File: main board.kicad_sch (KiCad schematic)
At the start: 1 part

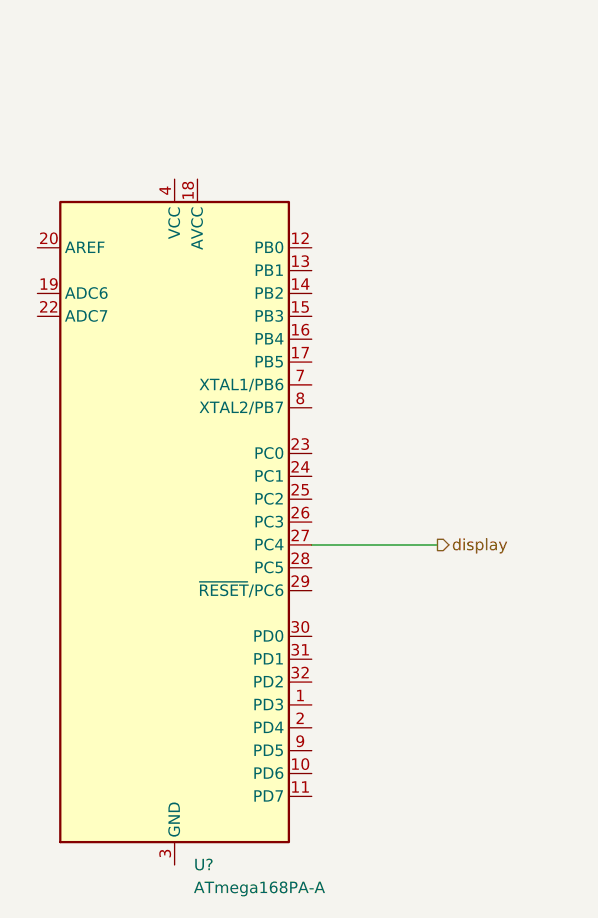
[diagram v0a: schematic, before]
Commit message: added display
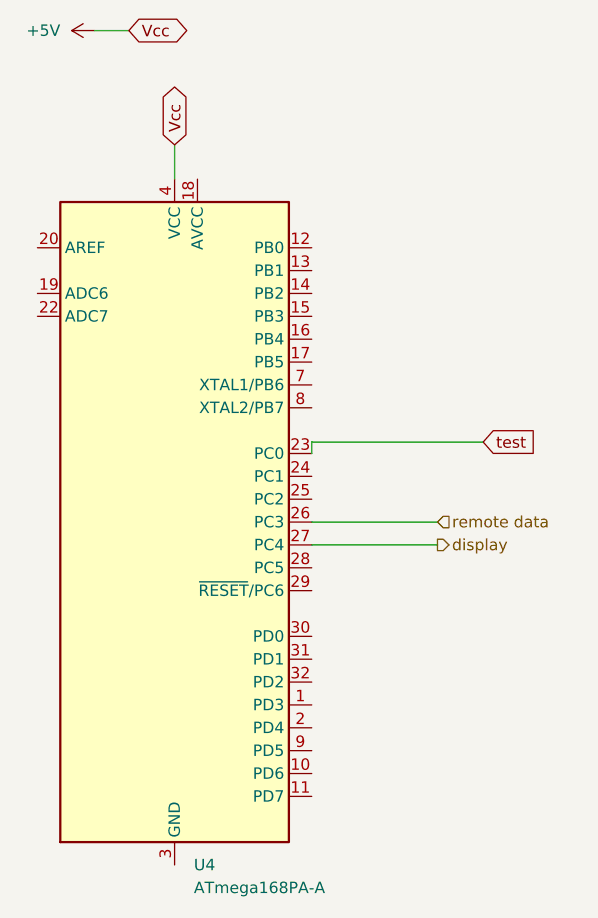
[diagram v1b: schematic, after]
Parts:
- gave numbers to parts that had none: 1
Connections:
- net test: now reaches U4.23 (PC0)
- net remote data: now reaches U4.26 (PC3)
- net +5V: now reaches U4.4 (VCC), U4.6 (VCC)
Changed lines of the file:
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@@
+	(wire
+		(pts
+			(xy 143.51 55.88) (xy 143.51 52.07)
+		)
+		(stroke
+			(width 0)
+			(type default)
+		)
+	)
+	(wire
+		(pts
+			(xy 134.62 39.37) (xy 138.43 39.37)
+		)
+		(stroke
+			(width 0)
+			(type default)
+		)
+	)
 	(wire
 		(pts
@@
 			(width 0)
 			(type default)
+		)
+	)
+	(wire
+		(pts
+			(xy 158.75 93.98) (xy 172.72 93.98)
+		)
+		(stroke
+			(width 0)
+			(type default)
+		)
+	)
+	(wire
+		(pts
+			(xy 158.75 85.09) (xy 158.75 86.36)
+		)
+		(stroke
+			(width 0)
+			(type default)
+		)
+	)
+	(wire
+		(pts
+			(xy 177.8 85.09) (xy 158.75 85.09)
+		)
+		(stroke
+			(width 0)
+			(type default)
+		)
+	)
+	(global_label "Vcc"
+		(shape bidirectional)
+		(at 138.43 39.37 0)
+		(fields_autoplaced yes)
+		(effects
+			(font
+				(size 1.27 1.27)
+			)
+			(justify left)
+		)
+		(property "Intersheetrefs" "${INTERSHEET_REFS}"
+			(at 145.7923 39.37 0)
+			(hide yes)
+			(show_name no)
+			(do_not_autoplace no)
+			(effects
+				(font
+					(size 1.27 1.27)
+				)
+				(justify left)
+			)
+		)
+	)
+	(global_label "test"
+		(shape input)
+		(at 177.8 85.09 0)
+		(fields_autoplaced yes)
+		(effects
+			(font
+				(size 1.27 1.27)
+			)
+			(justify left)
+		)
+		(property "Intersheetrefs" "${INTERSHEET_REFS}"
+			(at 184.3533 85.09 0)
+			(hide yes)
+			(show_name no)
+			(do_not_autoplace no)
+			(effects
+				(font
+					(size 1.27 1.27)
+				)
+				(justify left)
+			)
+		)
+	)
+	(global_label "Vcc"
+		(shape bidirectional)
+		(at 143.51 52.07 90)
+		(fields_autoplaced yes)
+		(effects
+			(font
+				(size 1.27 1.27)
+			)
+			(justify left)
+		)
+		(property "Intersheetrefs" "${INTERSHEET_REFS}"
+			(at 143.51 44.7077 90)
+			(hide yes)
+			(show_name no)
+			(do_not_autoplace no)
+			(effects
+				(font
+					(size 1.27 1.27)
+				)
+				(justify left)
+			)
 		)
 	)
@@
 		(shape output)
 		(at 172.72 96.52 0)
+		(effects
+			(font
+				(size 1.27 1.27)
+			)
+			(justify left)
+		)
+	)
+	(hierarchical_label "remote data"
+		(shape input)
+		(at 172.72 93.98 0)
 		(effects
 			(font
@@
 		(dnp no)
 		(fields_autoplaced yes)
-		(property "Reference" "U?"
+		(property "Reference" "U4"
 			(at 145.6533 132.08 0)
 			(show_name no)
@@
 			(project "First AIR Purifier"
 				(path "/08c08a39-65ea-48bd-a8aa-f7933860973b/c2e3a2bf-2352-4393-a448-602a3df1c4cc"
-					(reference "U?")
+					(reference "U4")
 					(unit 1)
 				)
+			)
+		)
+	)
+	(symbol
+		(lib_id "power:+5V")
+		(at 134.62 39.37 90)
+		(unit 1)
+		(body_style 1)
+		(exclude_from_sim no)
+		(in_bom yes)
+		(on_board yes)
+		(in_pos_files yes)
+		(dnp no)
+		(fields_autoplaced yes)
+		(property "Reference" "#PWR05"
+			(at 138.43 39.37 0)
+			(hide yes)
+			(show_name no)
+			(do_not_autoplace no)
+			(effects
+				(font
+					(size 1.27 1.27)
+				)
+			)
+		)
+		(property "Value" "+5V"
+			(at 130.81 39.3699 90)
+			(show_name no)
+			(do_not_autoplace no)
+			(effects
+				(font
+					(size 1.27 1.27)
+				)
+				(justify left)
+			)
+		)
+		(property "Footprint" ""
+			(at 134.62 39.37 0)
+			(hide yes)
+			(show_name no)
+			(do_not_autoplace no)
+			(effects
+				(font
+					(size 1.27 1.27)
+				)
+			)
+		)
+		(property "Datasheet" ""
+			(at 134.62 39.37 0)
+			(hide yes)
+			(show_name no)
+			(do_not_autoplace no)
+			(effects
+				(font
+					(size 1.27 1.27)
+				)
+			)
+		)
+		(property "Description" "Power symbol creates a global label with name \"+5V\""
+			(at 134.62 39.37 0)
+			(hide yes)
+			(show_name no)
+			(do_not_autoplace no)
+			(effects
+				(font
+					(size 1.27 1.27)
+				)
+			)
+		)
+		(pin "1"
+		)
+		(instances
+			(project "First AIR Purifier"
+				(path "/08c08a39-65ea-48bd-a8aa-f7933860973b/c2e3a2bf-2352-4393-a448-602a3df1c4cc"
+					(reference "#PWR05")
+					(unit 1)
+				)
